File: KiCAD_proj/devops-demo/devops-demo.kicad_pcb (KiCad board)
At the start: 2 copper layers, 52.7 x 41.3 mm, 14 parts, among them J1 Conn_PinHeader_FTDI_1x06_P2.5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, SW1 SWITCH_JS102011JCQN, SW2 BUTTON_B3SN, U1 ESP32-WROOM-32, U2 AMS1117-3.3

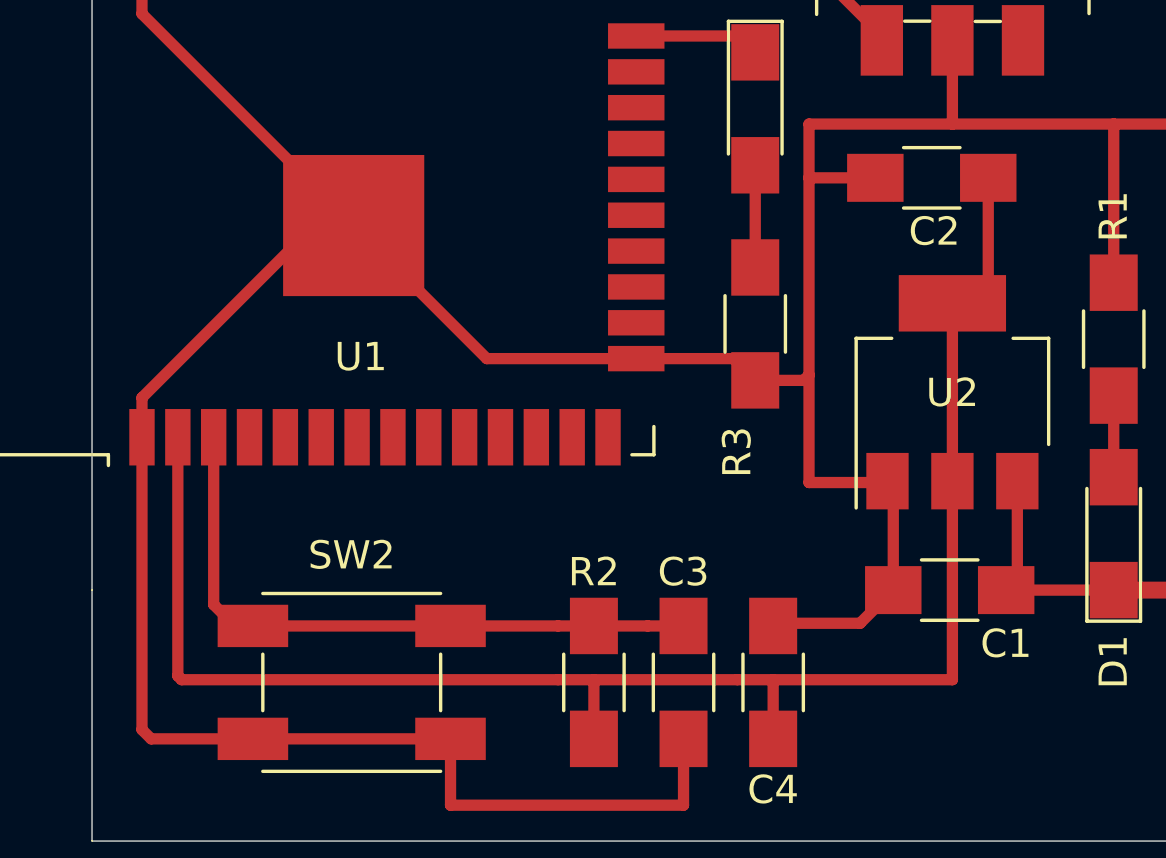
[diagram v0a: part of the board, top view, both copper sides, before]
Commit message: Changed power line widths
Using net class
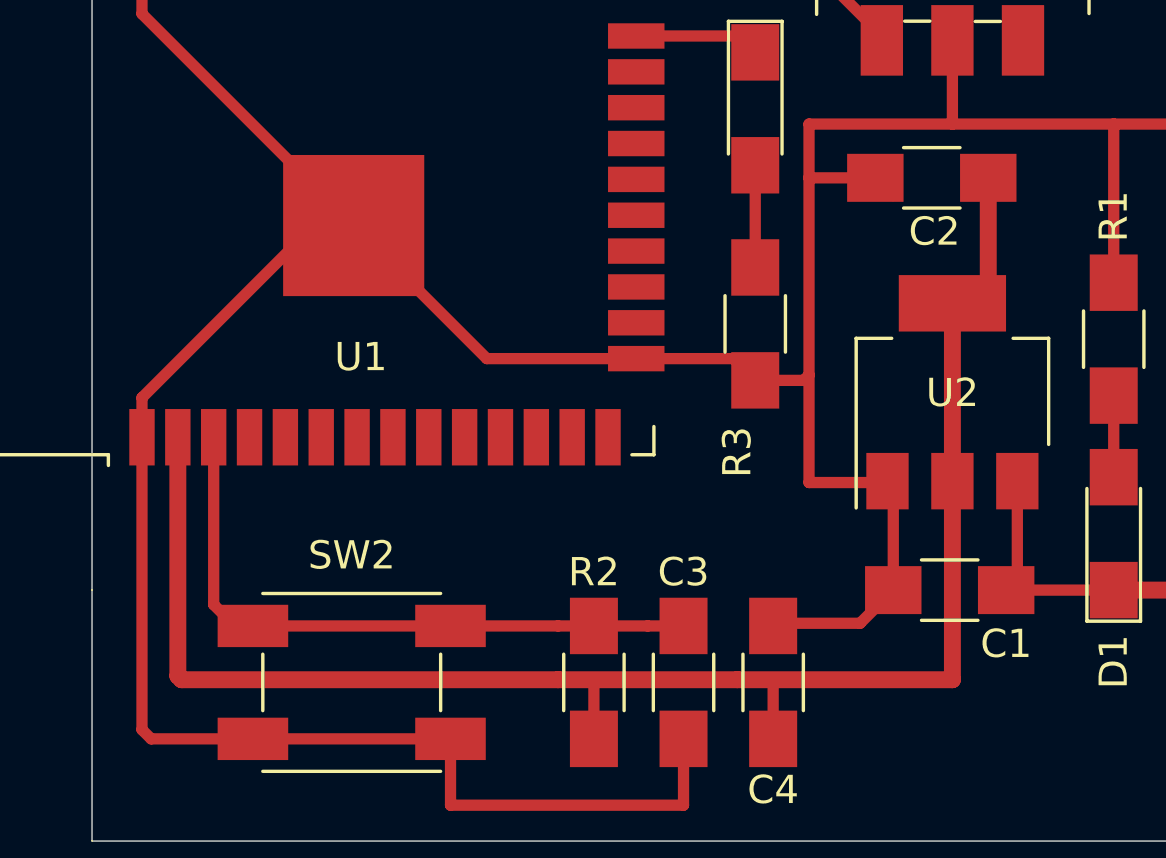
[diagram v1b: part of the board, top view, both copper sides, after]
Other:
- net class Power added: clearance 0.2, trace_width 0.6, via_dia 0.8, via_drill 0.4

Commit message: Update devops-demo.kicad_pcb
Mango
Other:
- board text added: "MANGO"
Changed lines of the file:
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@@
   (general
     (thickness 1.6)
-    (drawings 7)
+    (drawings 8)
     (tracks 79)
     (zones 0)
@@
     )
   )
+  (gr_text MANGO (at 173.355 117.475) (layer F.Cu)
+    (effects (font (size 1.5 1.5) (thickness 0.3)))
+  )
   (gr_line (start 177.8 77.47) (end 177.8 81.915) (layer Edge.Cuts) (width 0.05))
